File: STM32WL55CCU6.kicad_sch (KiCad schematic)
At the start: 25 parts, among them J6 BOOT0_Jumper, SW3 Switch_NX3L1T3157GMZ, U4 STM32WL55CCU6

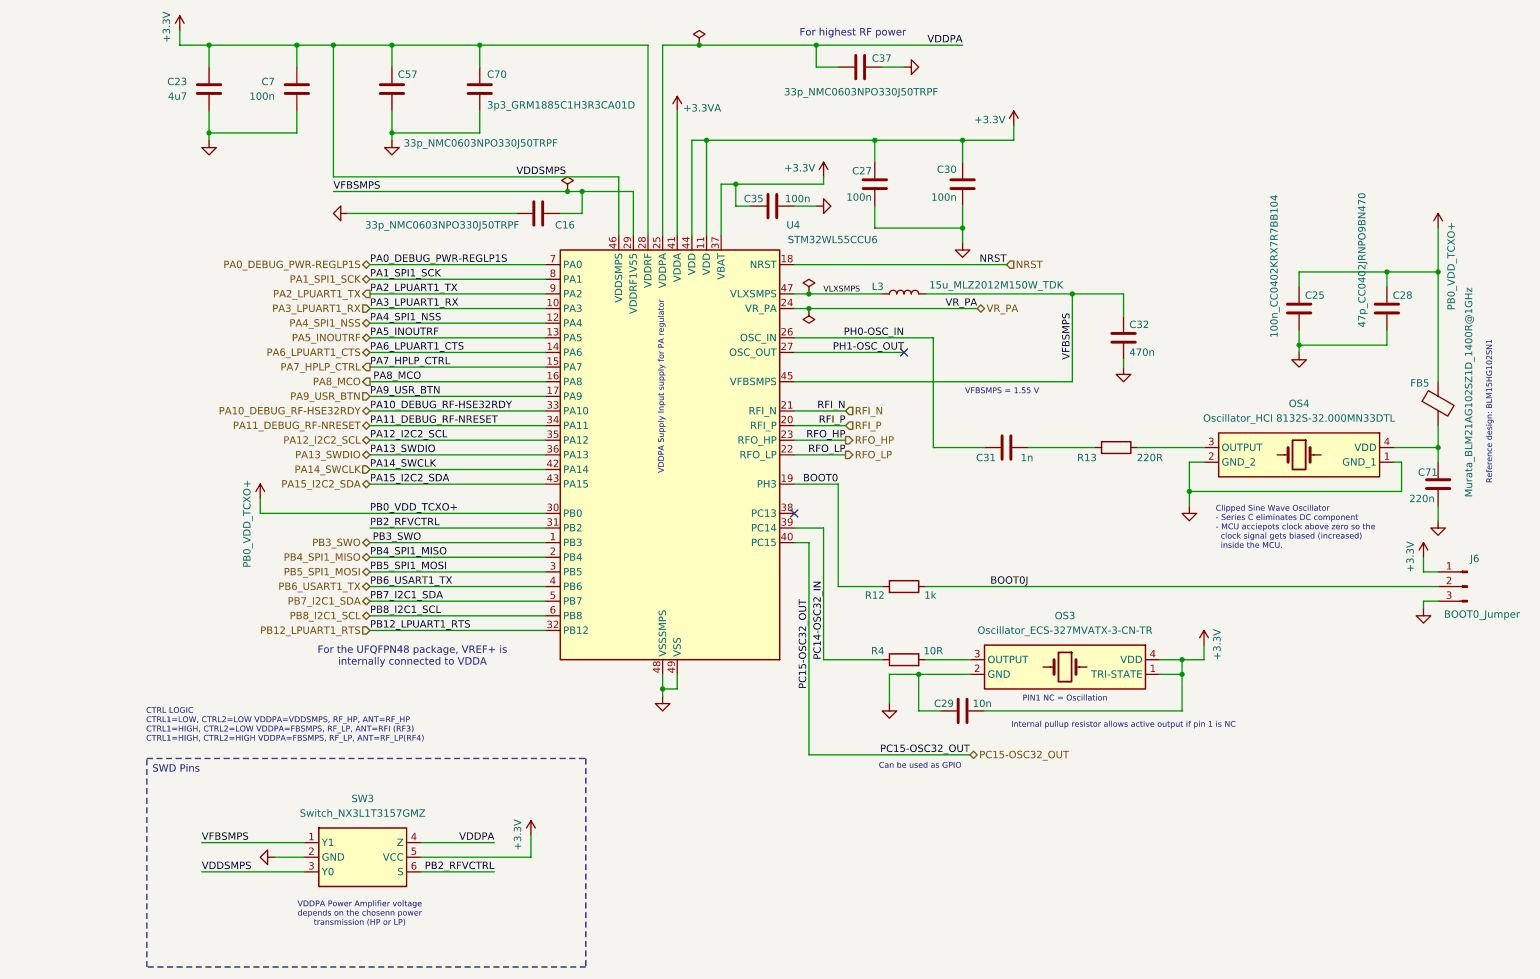
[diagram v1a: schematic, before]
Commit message: Schematics Update
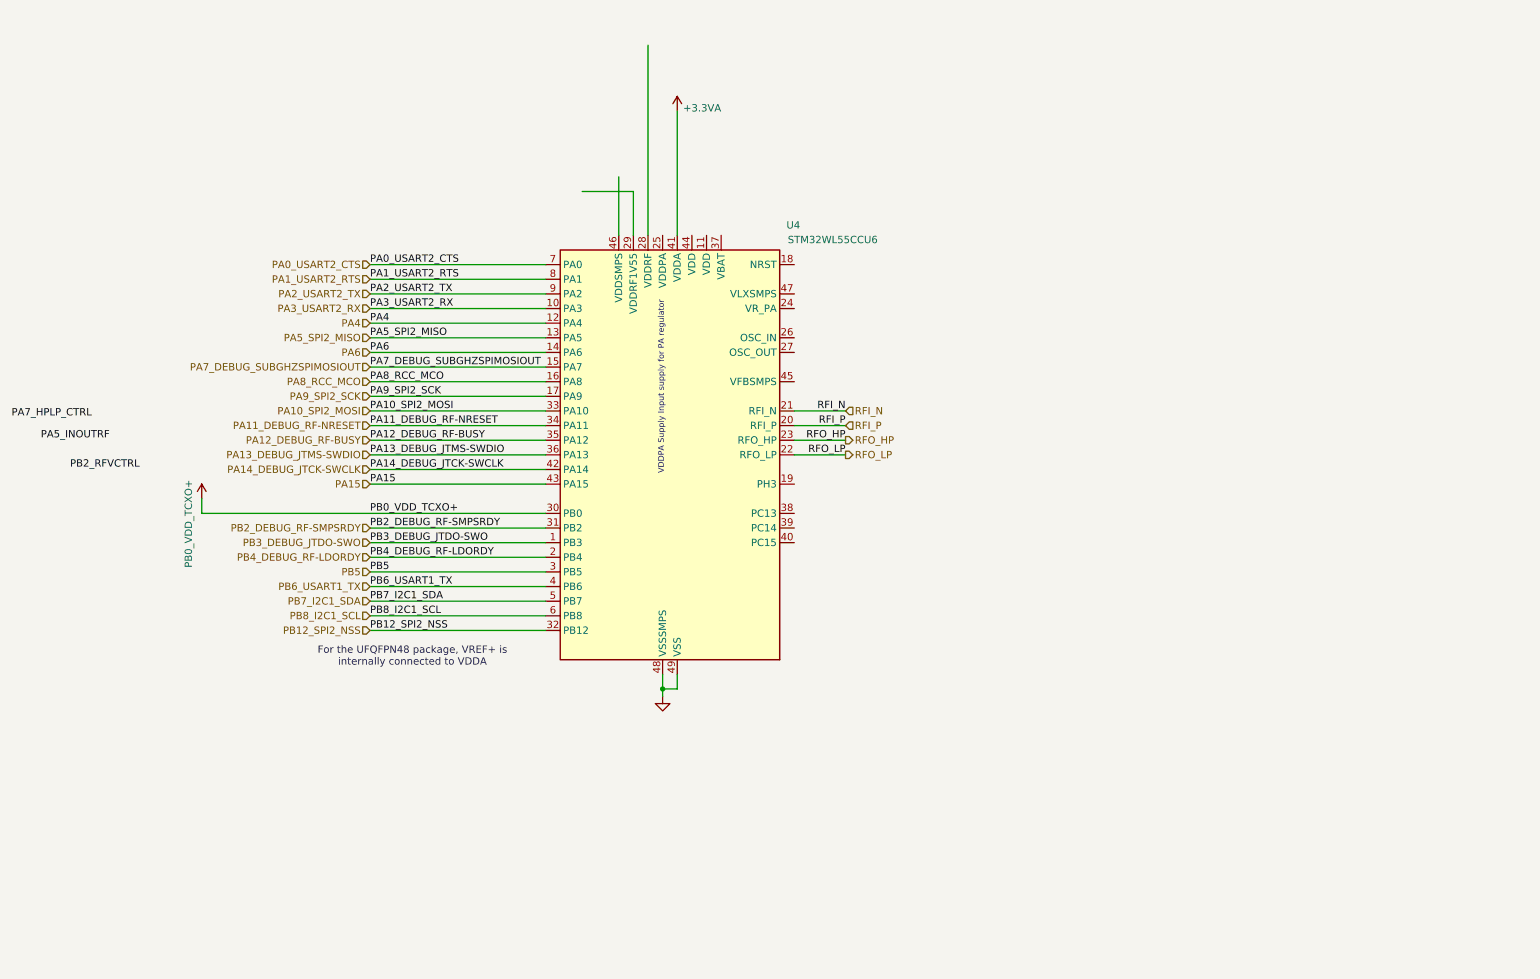
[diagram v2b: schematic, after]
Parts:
- removed C16, C37, C57: 33p_NMC0603NPO330J50TRPF, Capacitor_SMD:C_0603_1608Metric, symbol Device:C
- removed C23: 4u7, Capacitor_SMD:C_0805_2012Metric, symbol Device:C
- removed C25: 100n_CC0402KRX7R7BB104, Capacitor_SMD:C_0805_2012Metric, symbol Device:C
- removed C27, C30, C35, C7: 100n, Capacitor_SMD:C_0805_2012Metric, symbol Device:C
- removed C28: 47p_CC0402JRNPO9BN470, Capacitor_SMD:C_0805_2012Metric, symbol Device:C
- removed C29: 10n, Capacitor_SMD:C_0805_2012Metric, symbol Device:C
- removed C31: 1n, Capacitor_SMD:C_0805_2012Metric, symbol Device:C
- removed C32: 470n, Capacitor_SMD:C_0805_2012Metric, symbol Device:C
- removed C70: 3p3_GRM1885C1H3R3CA01D, Capacitor_SMD:C_0603_1608Metric, symbol Device:C
- removed C71: 220n, Capacitor_SMD:C_0805_2012Metric, symbol Device:C
- removed FB5: Murata_BLM21AG102SZ1D_1400R@1GHz, Capacitor_SMD:C_0805_2012Metric, symbol Device:FerriteBead
- removed J6: BOOT0_Jumper, Connector_PinHeader_2.54mm:PinHeader_1x03_P2.54mm_Vertical, symbol Connector:Conn_01x03_Pin
- removed L3: 15u_MLZ2012M150W_TDK, Inductor_SMD:L_0805_2012Metric_Pad1.15x1.40mm_HandSolder, symbol Device:L
- removed OS3: Oscillator_ECS-327MVATX-3-CN-TR, Personal_Project:Oscillator_ECS327MVATX3CNTR, symbol Personal_Projects:Oscillator_ECS-327MVATX-3-CN-TR
- removed OS4: Oscillator_HCI 8132S-32.000MN33DTL, Personal_Project:Oscillator_ECSTXO32CSMV320ANTR, symbol Personal_Projects:Oscillator_ECS-TXO-32CSMV-320-AN-TR
- removed R12: 1k, Resistor_SMD:R_0805_2012Metric, symbol Device:R
- removed R13: 220R, Resistor_SMD:R_0805_2012Metric, symbol Device:R
- removed R4: 10R, Resistor_SMD:R_0805_2012Metric, symbol Device:R
- removed SW3: Switch_NX3L1T3157GMZ, Personal_Project:Switch_NX3L1T3157GM115, symbol Personal_Projects:Switch_NX3L1T3157GM,115
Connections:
- net PA5_INOUTRF: no longer U4.13 (PA5)
- net PA7_HPLP_CTRL: no longer U4.15 (PA7)
- net PB2_RFVCTRL: no longer U4.31 (PB2)
- removed net +3.3V: U4.11 (VDD), U4.28 (VDDRF), U4.37 (VBAT), U4.44 (VDD), U4.46 (VDDSMPS)
- net BOOT0: no longer names the net of U4.19 (PH3)
- net NRST: no longer names the net of U4.18 (NRST)
- net PA0_DEBUG_PWR-REGLP1S renamed PA0_USART2_CTS
- net PA10_DEBUG_RF-HSE32RDY renamed PA10_SPI2_MOSI
- net PA12_I2C2_SCL renamed PA12_DEBUG_RF-BUSY
- net PA13_SWDIO renamed PA13_DEBUG_JTMS-SWDIO
- net PA14_SWCLK renamed PA14_DEBUG_JTCK-SWCLK
- net PA15_I2C2_SDA renamed PA15
- net PA1_SPI1_SCK renamed PA1_USART2_RTS
- net PA2_LPUART1_TX renamed PA2_USART2_TX
- net PA3_LPUART1_RX renamed PA3_USART2_RX
- net PA4_SPI1_NSS renamed PA4
- net PA6_LPUART1_CTS renamed PA6
- net PA8_MCO renamed PA8_RCC_MCO
- net PA9_USR_BTN renamed PA9_SPI2_SCK
- net PB12_LPUART1_RTS renamed PB12_SPI2_NSS
- net PB3_SWO renamed PB3_DEBUG_JTDO-SWO
- net PB4_SPI1_MISO renamed PB4_DEBUG_RF-LDORDY
- net PB5_SPI1_MOSI renamed PB5
- net PC14-OSC32_IN: no longer names the net of U4.39 (PC14)
- net PC15-OSC32_OUT: no longer names the net of U4.40 (PC15)
- net PH0-OSC_IN: no longer names the net of U4.26 (OSC_IN)
- net PH1-OSC_OUT: no longer names the net of U4.27 (OSC_OUT)
- net VDDPA: no longer names the net of U4.25 (VDDPA)
- net VFBSMPS: no longer names the net of U4.29 (VDDRF1V55)
- net VFBSMPS: no longer U4.45 (VFBSMPS)
- net VLXSMPS: no longer names the net of U4.47 (VLXSMPS)
- net VR_PA: no longer names the net of U4.24 (VR_PA)
- new net PA5_SPI2_MISO: U4.13 (PA5)
- new net PA7_DEBUG_SUBGHZSPIMOSIOUT: U4.15 (PA7)
- new net PB2_DEBUG_RF-SMPSRDY: U4.31 (PB2)
- no-connect marks 2 -> 0
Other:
- note removed: "CTRL LOGIC CTRL1=LOW, CTRL2=LOW VDDPA=VDDSMPS, RF_HP, ANT=RF_HP CTRL1=HIGH, CTRL2=LOW VDDPA=FBSMPS, RF_LP, ANT=RFI (RF3) CTRL1=HIGH, CTRL2=HIGH VDDPA=FBSMPS, RF_LP, ANT=RF_LP(RF4)"
- note removed: "Can be used as GPIO"
- note removed: "Clipped Sine Wave Oscillator - Series C eliminates DC component - MCU acciepots clock above zero so the clock signal gets biased (increased) inside the MCU."
- note removed: "For highest RF power"
- note removed: "Internal pullup resistor allows active output if pin 1 is NC"
- note removed: "PIN1 NC = Oscillation"
- note removed: "Reference design: BLM15HG102SN1"
- note removed: "VDDPA Power Amplifier voltage depends on the chosenn power transmission (HP or LP)"
- note removed: "VFBSMPS = 1.55 V"
